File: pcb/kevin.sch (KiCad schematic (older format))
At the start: 83 parts, among them J1 battery, J2 joystick_analogic, J3 eink, J4 to-trackball-side, J5 trackball-side, SW00 SW_Push, SW01 SW_Push, SW02 SW_Push, SW03 SW_Push, SW04 SW_Push, SW05 SW_Push, SW10 SW_Push, SW11 SW_Push, SW12 SW_Push, SW13 SW_Push, SW14 SW_Push, SW15 SW_Push, SW20 SW_Push, SW21 SW_Push, SW22 SW_Push, SW23 SW_Push, SW24 SW_Push, SW25 SW_Push, SW32 SW_Push, SW33 SW_Push, SW34 SW_Push, SW35 SW_Push, U1 nice_nano, U2 XC6206P202MR-G, U3 PMW3360DM-T2QU

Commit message: Adding reversible footprints and initialize readme
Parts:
- J1: footprint random-keyboard-parts:JST-SR-3 -> kevin:JST-SR-3_reversible
- J2: footprint Connector_FFC-FPC:Molex_200528-0040_1x04-1MP_P1.00mm_Horizontal -> kevin:Molex_200528-0040_1x04-1MP_P1.00mm_Horizontal_reversible
- SW_4dir1: footprint kevin:Alpsalpine skrhade010 -> kevin:Alpsalpine_skrhade010_reversible
- SW_IO_1: footprint Button_Switch_SMD:SW_SPDT_CK-JS102011SAQN -> kevin:SW_SPDT_CK-JS102011SAQN_reversible
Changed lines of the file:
@@
 F 0 "J2" H 3555 4617 50  0000 L CNN
 F 1 "joystick_analogic" H 3555 4526 50  0000 L CNN
-F 2 "Connector_FFC-FPC:Molex_200528-0040_1x04-1MP_P1.00mm_Horizontal" H 3475 4625 50  0001 C CNN
+F 2 "kevin:Molex_200528-0040_1x04-1MP_P1.00mm_Horizontal_reversible" H 3475 4625 50  0001 C CNN
 F 3 "~" H 3475 4625 50  0001 C CNN
 	1    3475 4625
@@
 F 0 "SW_IO_1" H 6725 5560 50  0000 C CNN
 F 1 "SW_SPST" H 6725 5469 50  0000 C CNN
-F 2 "Button_Switch_SMD:SW_SPDT_CK-JS102011SAQN" H 6725 5325 50  0001 C CNN
+F 2 "kevin:SW_SPDT_CK-JS102011SAQN_reversible" H 6725 5325 50  0001 C CNN
 F 3 "~" H 6725 5325 50  0001 C CNN
 	1    6725 5325
@@
 F 0 "J1" H 7205 5317 50  0000 L CNN
 F 1 "battery" H 7205 5226 50  0000 L CNN
-F 2 "random-keyboard-parts:JST-SR-3" H 7125 5325 50  0001 C CNN
+F 2 "kevin:JST-SR-3_reversible" H 7125 5325 50  0001 C CNN
 F 3 "~" H 7125 5325 50  0001 C CNN
 	1    7125 5325
@@
 F 0 "SW_4dir1" H 1725 5475 50  0000 C CNN
 F 1 "SW_4dir-push" H 1725 5384 50  0000 C CNN
-F 2 "kevin:Alpsalpine skrhade010" H 1625 5700 50  0001 C CNN
+F 2 "kevin:Alpsalpine_skrhade010_reversible" H 1625 5700 50  0001 C CNN
 F 3 "https://tech.alpsalpine.com/prod/e/html/multicontrol/switch/skrh/skrhade010.html" H 1625 5700 50  0001 C CNN
 	1    1725 5100

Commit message: Adjust components (battery footprint, JSR, corrections) Add temporary BOM Correction of battery component (remove kicad complaint)
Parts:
- BT1: footprint (none) -> kevin:Battery_holder_reversible; symbol Device:Battery_Cell -> kevin:Battery_Cell
- C20: value 100nF -> 0.1uF
- J1: footprint kevin:JST-SR-3_reversible -> kevin:JST_SH_SM02B-SRSS-TB_1x02-1MP_P1.00mm_Horizontal_reversible
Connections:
- net GND: no longer BT1.2 (-)
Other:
- note added: "lithium battery 3.7V\n(connected to J1)"
- note removed: "lithium battery 3.7V"
- moved on the sheet: SW_RST_1, U2
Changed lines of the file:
@@
 Text Notes 725  6550 0    50   ~ 0
 connector (pogo)\nfrom main pcb -->
-Text Notes 9935 4965 0    50   Italic 0
-(used for PMW3360)
 $Comp
 L Connector_Generic:Conn_01x30 J3
@@
 	0    1    1    0
 $EndComp
-$Comp
-L Device:C_Small C12
-U 1 1 61667101
-P 10650 3325
-F 0 "C12" V 10421 3325 50  0000 C CNN
-F 1 "1uF" V 10512 3325 50  0000 C CNN
-F 2 "kevin:C_0805_reversible" H 10650 3325 50  0001 C CNN
-F 3 "~" H 10650 3325 50  0001 C CNN
-	1    10650 3325
-	0    1    1    0
-$EndComp
 Text GLabel 10750 1825 0    50   Input ~ 0
 eink_dc
@@
 Text Notes 8700 725  0    118  ~ 24
 Display
-Text Notes 9750 4975 0    50   ~ 0
-LDO
-$Comp
-L power:GND #PWR0114
-U 1 1 611D91CD
-P 10375 5650
-F 0 "#PWR0114" H 10375 5400 50  0001 C CNN
-F 1 "GND" V 10380 5522 50  0000 R CNN
-F 2 "" H 10375 5650 50  0001 C CNN
-F 3 "" H 10375 5650 50  0001 C CNN
-	1    10375 5650
-	1    0    0    -1
-$EndComp
-Text GLabel 10675 5350 2    50   Output ~ 0
-vdd_2v
-$Comp
-L Regulator_Linear:XC6206PxxxMR U2
-U 1 1 611AA876
-P 10375 5350
-F 0 "U2" H 10375 5592 50  0000 C CNN
-F 1 "XC6206P202MR-G" H 10375 5501 50  0000 C CNN
-F 2 "Package_TO_SOT_SMD:SOT-23" H 10375 5575 50  0001 C CIN
-F 3 "https://www.torexsemi.com/file/xc6206/XC6206.pdf" H 10375 5350 50  0001 C CNN
-	1    10375 5350
-	1    0    0    -1
-$EndComp
 Text GLabel 6600 1875 0    50   Output ~ 0
 spi_clk
@@
 Text Notes 6225 4975 0    50   ~ 0
 on/off switch
-Text Notes 8800 4975 0    50   ~ 0
-lithium battery 3.7V
 Connection ~ 6600 1675
 Text GLabel 7300 3075 3    50   Input ~ 0
@@
 Text GLabel 7000 3075 3    50   Output ~ 0
 spi_reset
-$Comp
-L power:GND #PWR0112
-U 1 1 611517EC
-P 9050 5575
-F 0 "#PWR0112" H 9050 5325 50  0001 C CNN
-F 1 "GND" V 9055 5447 50  0000 R CNN
-F 2 "" H 9050 5575 50  0001 C CNN
-F 3 "" H 9050 5575 50  0001 C CNN
-	1    9050 5575
-	1    0    0    -1
-$EndComp
-$Comp
-L power:PWR_FLAG #FLG0101
-U 1 1 61150920
-P 9050 5275
-F 0 "#FLG0101" H 9050 5350 50  0001 C CNN
-F 1 "PWR_FLAG" H 9050 5448 50  0000 C CNN
-F 2 "" H 9050 5275 50  0001 C CNN
-F 3 "~" H 9050 5275 50  0001 C CNN
-	1    9050 5275
-	1    0    0    -1
-$EndComp
 Text GLabel 7150 3075 3    50   Input ~ 0
 eink_busy
@@
 Text Notes 6225 4550 0    118  ~ 24
 Power & reset
-Text Notes 7655 4975 0    50   ~ 0
-reset button
 Text GLabel 8000 1775 2    50   Output ~ 0
 vdd_3v3
@@
 	0    -1   -1   0
 $EndComp
-$Comp
-L Switch:SW_Push SW_RST_1
-U 1 1 610096B7
-P 8125 5375
-F 0 "SW_RST_1" H 8125 5660 50  0000 C CNN
-F 1 "SW_Push" H 8125 5569 50  0000 C CNN
-F 2 "kevin:SKQGADE010_reversible" H 8125 5575 50  0001 C CNN
-F 3 "~" H 8125 5575 50  0001 C CNN
-	1    8125 5375
-	1    0    0    -1
-$EndComp
-$Comp
-L power:GND #PWR0104
-U 1 1 6100A999
-P 8325 5375
-F 0 "#PWR0104" H 8325 5125 50  0001 C CNN
-F 1 "GND" V 8330 5247 50  0000 R CNN
-F 2 "" H 8325 5375 50  0001 C CNN
-F 3 "" H 8325 5375 50  0001 C CNN
-	1    8325 5375
-	0    -1   -1   0
-$EndComp
 Wire Wire Line
 	6925 5425 6925 5525
@@
 F 0 "J1" H 7205 5317 50  0000 L CNN
 F 1 "battery" H 7205 5226 50  0000 L CNN
-F 2 "kevin:JST-SR-3_reversible" H 7125 5325 50  0001 C CNN
+F 2 "kevin:JST_SH_SM02B-SRSS-TB_1x02-1MP_P1.00mm_Horizontal_reversible" H 7125 5325 50  0001 C CNN
 F 3 "~" H 7125 5325 50  0001 C CNN
 	1    7125 5325
-	1    0    0    -1
-$EndComp
-$Comp
-L Device:Battery_Cell BT1
-U 1 1 60FE2446
-P 9050 5475
-F 0 "BT1" H 9168 5571 50  0000 L CNN
-F 1 "Battery_Cell" H 9168 5480 50  0000 L CNN
-F 2 "" V 9050 5535 50  0001 C CNN
-F 3 "~" V 9050 5535 50  0001 C CNN
-	1    9050 5475
 	1    0    0    -1
 $EndComp
@@
 P 3500 6700
 F 0 "C20" V 3271 6700 50  0000 C CNN
-F 1 "100nF" V 3362 6700 50  0000 C CNN
+F 1 "0.1uF" V 3362 6700 50  0000 C CNN
 F 2 "Capacitor_SMD:C_0805_2012Metric_Pad1.18x1.45mm_HandSolder" H 3500 6700 50  0001 C CNN
 F 3 "~" H 3500 6700 50  0001 C CNN
@@
 Wire Wire Line
 	2475 1675 3325 1675
-Text GLabel 10075 5350 0    50   Input ~ 0
-vdd_3v3
 Wire Notes Line
 	475  5775 6000 5775
@@
 Text Notes 9850 2100 0    39   Italic 0
 4-line SPI
-Text GLabel 7925 5375 0    50   Output ~ 0
-reset
 $Comp
 L Device:R R02
@@
 Text GLabel 8000 2575 2    50   Input ~ 0
 col5
+$Comp
+L Device:C_Small C12
+U 1 1 61667101
+P 10650 3325
+F 0 "C12" V 10421 3325 50  0000 C CNN
+F 1 "1uF" V 10512 3325 50  0000 C CNN
+F 2 "kevin:C_0805_reversible" H 10650 3325 50  0001 C CNN
+F 3 "~" H 10650 3325 50  0001 C CNN
+	1    10650 3325
+	0    1    1    0
+$EndComp
+Text Notes 8630 4950 0    50   ~ 0
+reset button
+Text Notes 9910 4940 0    50   Italic 0
+(used for PMW3360)
+Text Notes 9725 4950 0    50   ~ 0
+LDO
+Text Notes 7600 5025 0    50   ~ 0
+lithium battery 3.7V\n(connected to J1)
+$Comp
+L power:GND #PWR0114
+U 1 1 611D91CD
+P 10375 5675
+F 0 "#PWR0114" H 10375 5425 50  0001 C CNN
+F 1 "GND" V 10380 5547 50  0000 R CNN
+F 2 "" H 10375 5675 50  0001 C CNN
+F 3 "" H 10375 5675 50  0001 C CNN
+	1    10375 5675
+	1    0    0    -1
+$EndComp
+Text GLabel 10675 5375 2    50   Output ~ 0
+vdd_2v
+$Comp
+L Regulator_Linear:XC6206PxxxMR U2
+U 1 1 611AA876
+P 10375 5375
+F 0 "U2" H 10375 5617 50  0000 C CNN
+F 1 "XC6206P202MR-G" H 10375 5526 50  0000 C CNN
+F 2 "Package_TO_SOT_SMD:SOT-23" H 10375 5600 50  0001 C CIN
+F 3 "https://www.torexsemi.com/file/xc6206/XC6206.pdf" H 10375 5375 50  0001 C CNN
+	1    10375 5375
+	1    0    0    -1
+$EndComp
+$Comp
+L Switch:SW_Push SW_RST_1
+U 1 1 610096B7
+P 9100 5375
+F 0 "SW_RST_1" H 9100 5660 50  0000 C CNN
+F 1 "SW_Push" H 9100 5569 50  0000 C CNN
+F 2 "kevin:SKQGADE010_reversible" H 9100 5575 50  0001 C CNN
+F 3 "~" H 9100 5575 50  0001 C CNN
+	1    9100 5375
+	1    0    0    -1
+$EndComp
+$Comp
+L power:GND #PWR0104
+U 1 1 6100A999
+P 9300 5375
+F 0 "#PWR0104" H 9300 5125 50  0001 C CNN
+F 1 "GND" V 9305 5247 50  0000 R CNN
+F 2 "" H 9300 5375 50  0001 C CNN
+F 3 "" H 9300 5375 50  0001 C CNN
+	1    9300 5375
+	0    -1   -1   0
+$EndComp
+Text GLabel 10075 5375 0    50   Input ~ 0
+vdd_3v3
+Text GLabel 8900 5375 0    50   Output ~ 0
+reset
+$Comp
+L kevin:Battery_Cell BT1
+U 1 1 60FE2446
+P 7725 5425
+F 0 "BT1" H 7843 5521 50  0000 L CNN
+F 1 "Battery_Cell" H 7843 5430 50  0000 L CNN
+F 2 "kevin:Battery_holder_reversible" V 7725 5485 50  0001 C CNN
+F 3 "~" V 7725 5485 50  0001 C CNN
+	1    7725 5425
+	1    0    0    -1
+$EndComp
 $EndSCHEMATC

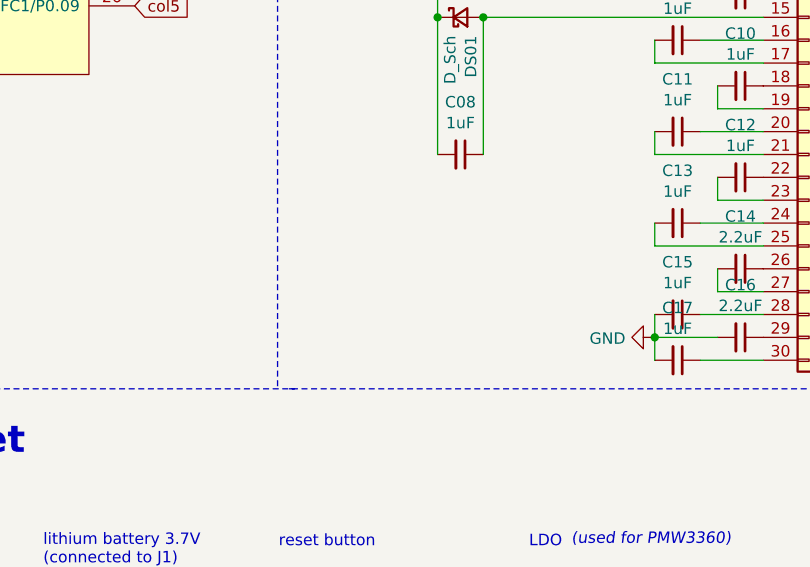
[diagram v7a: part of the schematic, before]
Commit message: Adding millmax connectors, submodule (kailh 3D, promicro 3D), screen
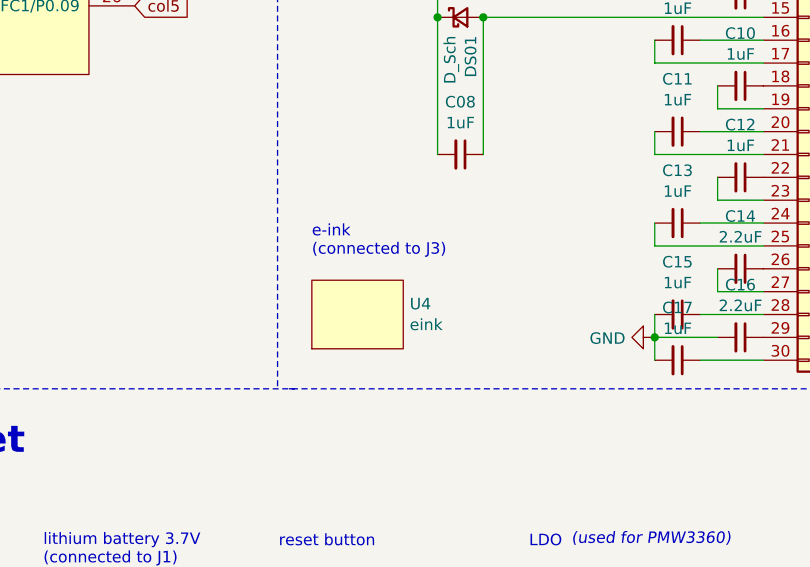
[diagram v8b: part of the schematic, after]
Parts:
- added U4: eink, kevin:Waveshare_eink_1.02 holder_reversible, symbol kevin:eink
- J4: footprint Connector_PinSocket_2.54mm:PinSocket_1x08_P2.54mm_Horizontal -> kevin:Mill-Max_319-10-108-40-080001_reversible
- J5: footprint Connector_PinSocket_2.54mm:PinSocket_1x08_P2.54mm_Horizontal -> kevin:Mill-Max_810-22-008-40-001101_reversible
- U3: footprint kevin:IC_PMW3360DM-T2QU -> kevin:PMW3360DM-T2QU
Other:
- note added: "e-ink\n(connected to J3)"
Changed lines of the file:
@@
 F 0 "J4" H 5230 4817 50  0000 L CNN
 F 1 "to-trackball-side" H 5230 4726 50  0000 L CNN
-F 2 "Connector_PinSocket_2.54mm:PinSocket_1x08_P2.54mm_Horizontal" H 5150 4825 50  0001 C CNN
-F 3 "~" H 5150 4825 50  0001 C CNN
+F 2 "kevin:Mill-Max_319-10-108-40-080001_reversible" H 5150 4825 50  0001 C CNN
+F 3 "https://www.mill-max.com/products/datasheet/sockets/319-10-108-40-080001" H 5150 4825 50  0001 C CNN
 	1    5150 4825
 	1    0    0    -1
@@
 F 0 "J5" H 1255 6992 50  0000 L CNN
 F 1 "trackball-side" H 1255 6901 50  0000 L CNN
-F 2 "Connector_PinSocket_2.54mm:PinSocket_1x08_P2.54mm_Horizontal" H 1175 7000 50  0001 C CNN
-F 3 "~" H 1175 7000 50  0001 C CNN
+F 2 "kevin:Mill-Max_810-22-008-40-001101_reversible" H 1175 7000 50  0001 C CNN
+F 3 "https://www.mill-max.com/products/datasheet/sockets/810-22-008-40-001101" H 1175 7000 50  0001 C CNN
 	1    1175 7000
 	-1   0    0    -1
@@
 F 0 "U3" H 4400 7440 50  0000 C CNN
 F 1 "PMW3360DM-T2QU" H 4400 7349 50  0000 C CNN
-F 2 "kevin:IC_PMW3360DM-T2QU" H 4425 7325 50  0001 C CNN
+F 2 "kevin:PMW3360DM-T2QU" H 4425 7325 50  0001 C CNN
 F 3 "https://www.epsglobal.com/Media-Library/EPSGlobal/Products/files/pixart/PMW3360DM-T2QU.pdf?ext=.pdf" H 4425 7325 50  0001 C CNN
 	1    4375 6925
@@
 	1    0    0    -1
 $EndComp
+Text Notes 8775 3675 0    50   ~ 0
+e-ink\n(connected to J3)
+$Comp
+L kevin:eink U4
+U 1 1 61326336
+P 8975 3925
+F 0 "U4" H 9203 3971 50  0000 L CNN
+F 1 "eink" H 9203 3880 50  0000 L CNN
+F 2 "kevin:Waveshare_eink_1.02 holder_reversible" H 8975 3925 50  0001 C CNN
+F 3 "https://www.waveshare.com/w/upload/2/2b/1.02inch-e-Paper_Specification.pdf" H 8975 3925 50  0001 C CNN
+	1    8975 3925
+	1    0    0    -1
+$EndComp
